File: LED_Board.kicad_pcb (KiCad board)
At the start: 2 copper layers, 75 x 75 mm, 5 parts, among them J2 Conn_01x02_Pin

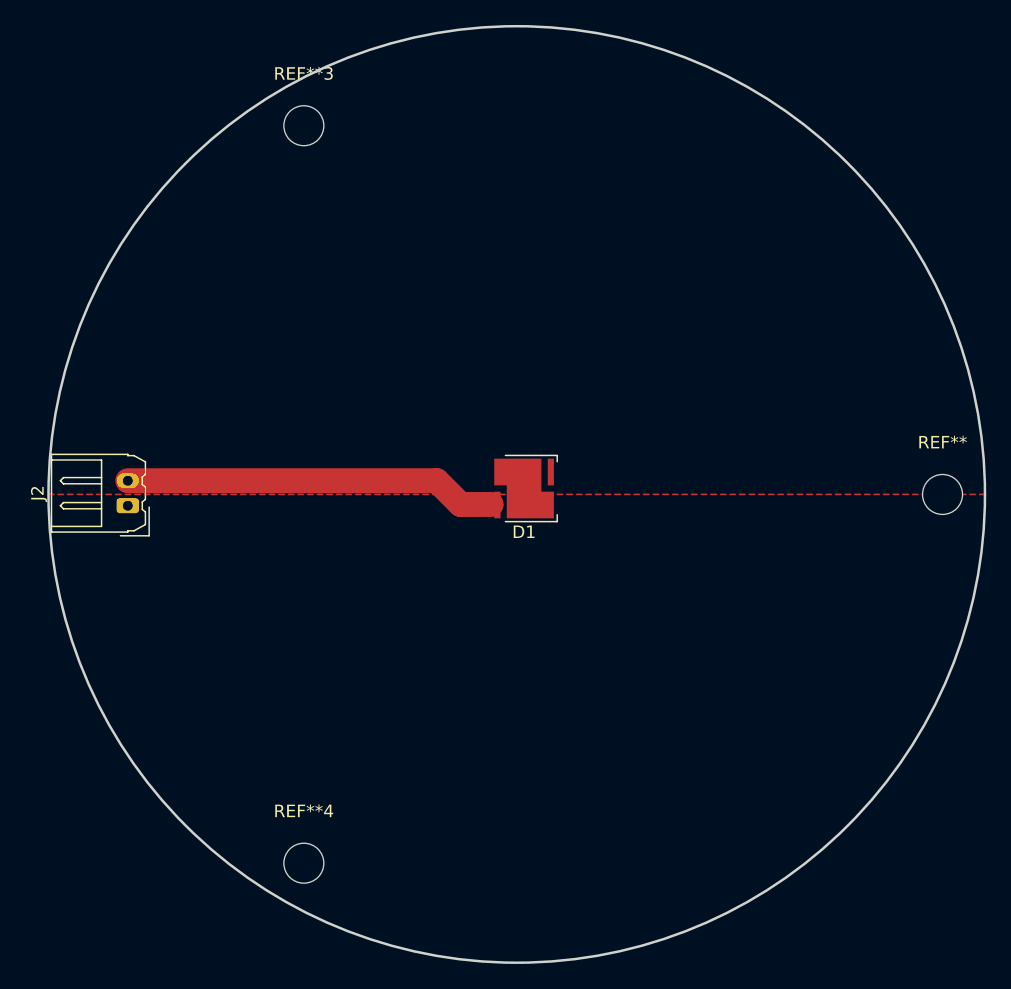
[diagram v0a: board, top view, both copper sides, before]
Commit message: Added 6 Warm LEDS and cleanup of silkscreen
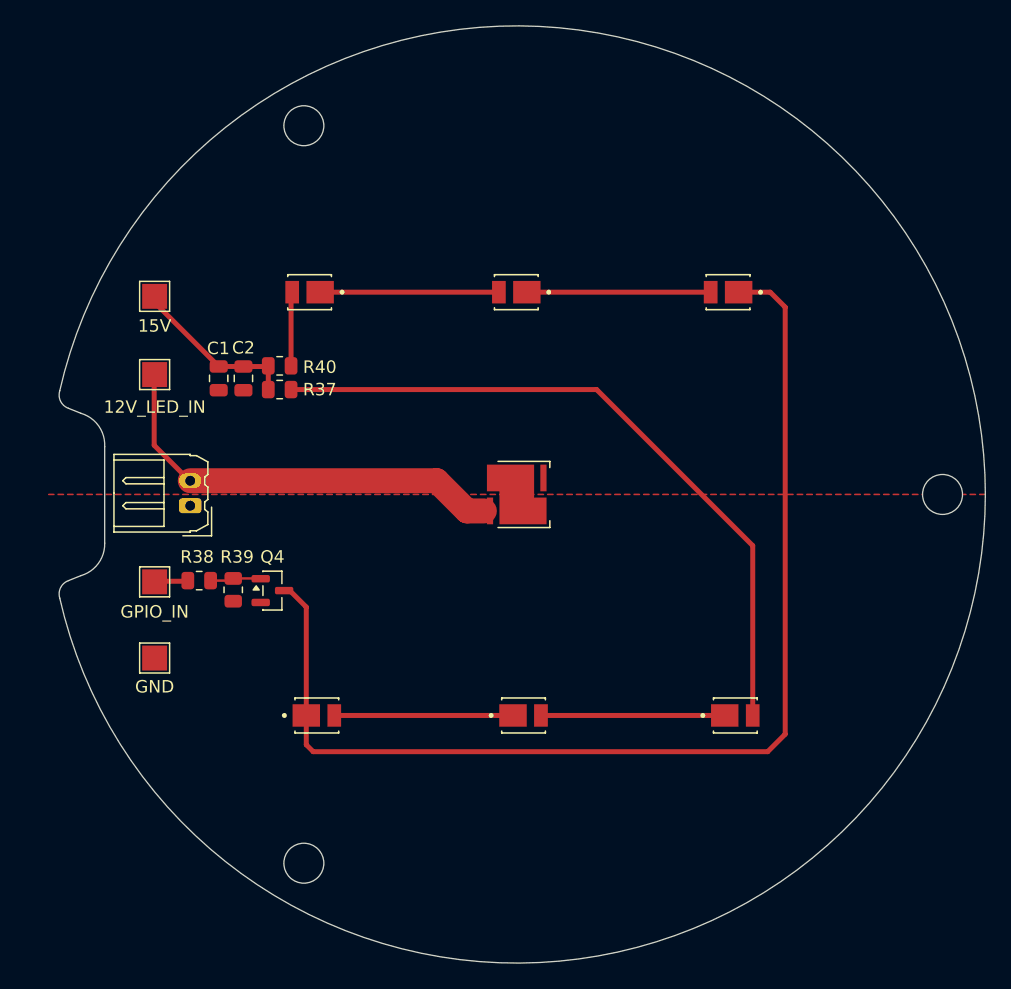
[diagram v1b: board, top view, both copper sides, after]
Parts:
- added C1: 100nF, Capacitor_SMD:C_0805_2012Metric, F.Cu at (145.0, 92.1)
- added C2: 1uF, Capacitor_SMD:C_0805_2012Metric, F.Cu at (147.0, 92.1)
- added D2: JB2835BWT-G-U40GA0000-N0000001, Library:LED_JB2835BWT-G-U40GA0000-N0000001, F.Cu at (169.4, 119.1)
- added D3: JB2835BWT-G-U40GA0000-N0000001, Library:LED_JB2835BWT-G-U40GA0000-N0000001, F.Cu at (152.9, 119.1)
- added D4: JB2835BWT-G-U40GA0000-N0000001, Library:LED_JB2835BWT-G-U40GA0000-N0000001, F.Cu at (152.3, 85.2)
- added D5: JB2835BWT-G-U40GA0000-N0000001, Library:LED_JB2835BWT-G-U40GA0000-N0000001, F.Cu at (168.9, 85.2)
- added D6: JB2835BWT-G-U40GA0000-N0000001, Library:LED_JB2835BWT-G-U40GA0000-N0000001, F.Cu at (185.8, 85.2)
- added D8: JB2835BWT-G-U40GA0000-N0000001, Library:LED_JB2835BWT-G-U40GA0000-N0000001, F.Cu at (186.4, 119.1)
- added Q4: AO3400A, Package_TO_SOT_SMD:SOT-23, F.Cu at (149.3, 109.1)
- added R37: 130R, Resistor_SMD:R_0805_2012Metric, F.Cu at (149.9, 93.0)
- added R38: 1K, Resistor_SMD:R_0805_2012Metric, F.Cu at (143.5, 108.3)
- added R39: 10K, Resistor_SMD:R_0805_2012Metric, F.Cu at (146.2, 109.0)
- added R40: 130R, Resistor_SMD:R_0805_2012Metric, F.Cu at (149.9, 91.1)
- added TP1: 15V, TestPoint:TestPoint_Pad_2.0x2.0mm, F.Cu at (139.9, 85.5)
- added TP2: GPIO_IN, TestPoint:TestPoint_Pad_2.0x2.0mm, F.Cu at (139.9, 108.4)
- added TP3: 12V_LED_IN, TestPoint:TestPoint_Pad_2.0x2.0mm, F.Cu at (139.9, 91.8)
- added TP4: GND, TestPoint:TestPoint_Pad_2.0x2.0mm, F.Cu at (139.9, 114.5)
- moved J2 5.00 mm to (142.8, 102.3)
- moved D1 0.76 mm to (168.9, 101.4)
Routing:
- net Net-(Q4-D): track 0.00 -> 90.4 mm
- net Net-(D8-PadA): track 0.00 -> 55.8 mm
- net Net-(D5-PadC): track 0.00 -> 14.7 mm
- net Net-(D2-PadA): track 0.00 -> 14.7 mm
- net Net-(D4-PadC): track 0.00 -> 14.3 mm
- net Net-(D2-PadC): track 0.00 -> 14.3 mm
- net +15V: track 0.00 -> 13.6 mm
- net Net-(D4-PadA): track 0.00 -> 5.94 mm
- net Net-(Q4-G): track 0.00 -> 4.10 mm
- net Net-(D1-A): track 30.2 -> 34.3 mm
- net /GPIO_IN: track 0.00 -> 3.18 mm
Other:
- board size 75 x 75 mm -> 74.2 x 75.1 mm

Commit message: Added LEDs and fixed V_IN trace widths
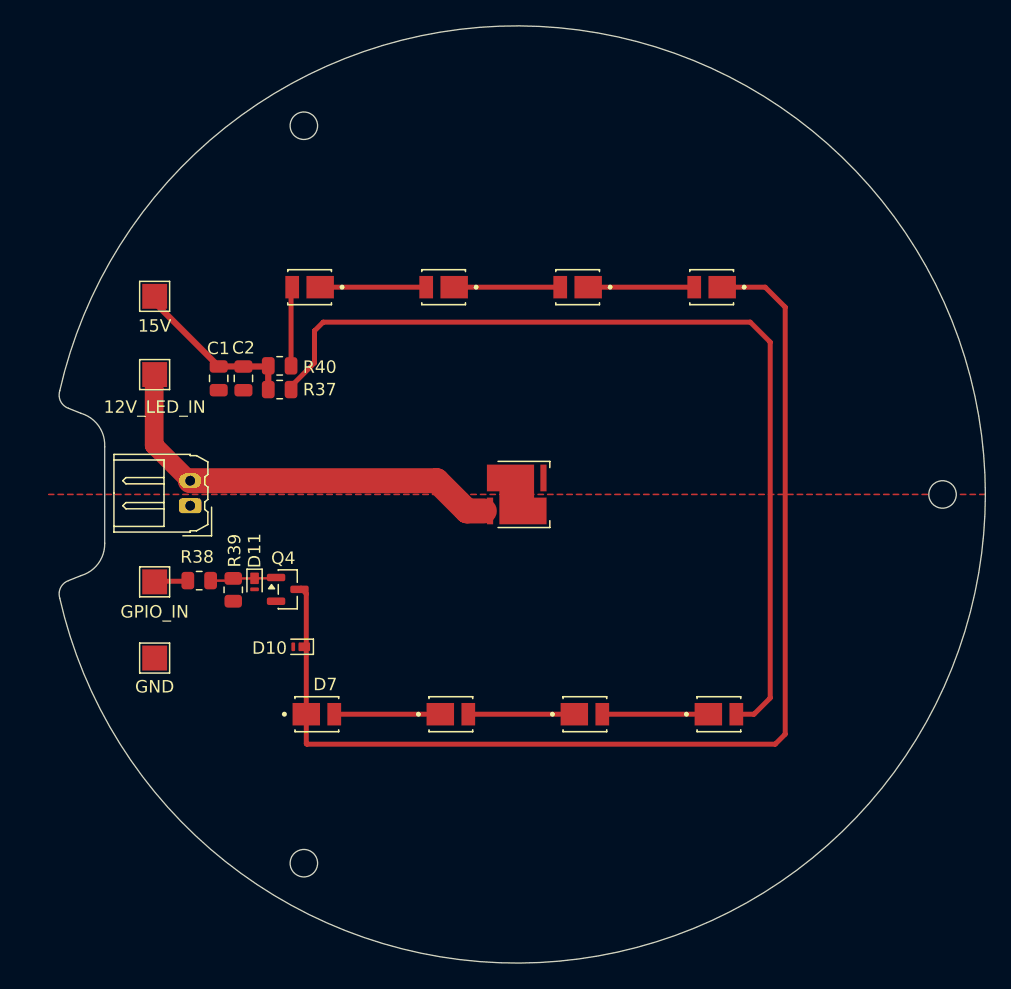
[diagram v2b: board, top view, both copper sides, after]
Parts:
- added D10: PTVS12VZ1USK, Diode_SMD:Nexperia_DSN1608-2_1.6x0.8mm, F.Cu at (151.6, 113.6)
- added D11: PTVS5V0Z1USKP, Diode_SMD:Nexperia_DSN1608-2_1.6x0.8mm, F.Cu at (147.9, 108.4)
- added D7: JB2835BWT-G-U40GA0000-N0000001, Library:LED_JB2835BWT-G-U40GA0000-N0000001, F.Cu at (152.9, 119.0)
- added D9: JB2835BWT-G-U40GA0000-N0000001, Library:LED_JB2835BWT-G-U40GA0000-N0000001, F.Cu at (184.5, 84.8)
- C1: value 100nF -> 100n
- C2: value 1uF -> 2u2
- R37, R40: value 130R -> 130
- REF**, REF**3, REF**4: value MountingHole_3.2mm_M3 -> MountingHole_2.2mm_M2; footprint MountingHole:MountingHole_3.2mm_M3 -> MountingHole:MountingHole_2.2mm_M2
- moved D6 12.1 mm to (173.8, 84.8)
- moved D3 10.7 mm to (163.6, 119.0)
- moved D5 5.84 mm to (163.0, 84.8)
- moved D2 4.91 mm to (174.4, 119.0)
- moved D8 1.32 mm to (185.1, 119.0)
- moved Q4 1.24 mm to (150.6, 109.0)
- moved D4 0.40 mm to (152.3, 84.8)
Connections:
- D3 pad C: Net-(Q4-D) -> Net-(D3-PadC)
- D6 pad C: Net-(Q4-D) -> Net-(D6-PadC)
- Q4 pad 3: Net-(Q4-D) -> Net-(D10-K)
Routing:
- net Net-(D10-K): track 0.00 -> 91.3 mm
- net Net-(Q4-D): track 90.4 -> 0.00 mm
- net Net-(D8-PadA): track 55.8 -> 74.7 mm
- net Net-(D6-PadC): track 0.00 -> 8.49 mm
- net Net-(D3-PadC): track 0.00 -> 8.49 mm
- net Net-(D2-PadA): track 14.7 -> 8.49 mm
- net Net-(D5-PadC): track 14.7 -> 8.49 mm
- net Net-(D4-PadC): track 14.3 -> 8.49 mm
- net Net-(D2-PadC): track 14.3 -> 8.49 mm
- net Net-(D11-K): track 4.10 -> 5.49 mm

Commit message: Apply all Fixes from Rev 1 (First Pass)
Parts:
- removed J2: Conn_01x02_Pin, Connector_Molex:Molex_Micro-Latch_53254-0270_1x02_P2.00mm_Horizontal
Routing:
- net GND: track 0.00 -> 3.10 mm, vias 0 -> 3
